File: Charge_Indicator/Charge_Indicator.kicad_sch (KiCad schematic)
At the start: 54 parts, among them J1 PZ254-2-02-S, J2 1711725, J3 1711725, SW1 SSSS811101, U1 TLV74033PDQNR

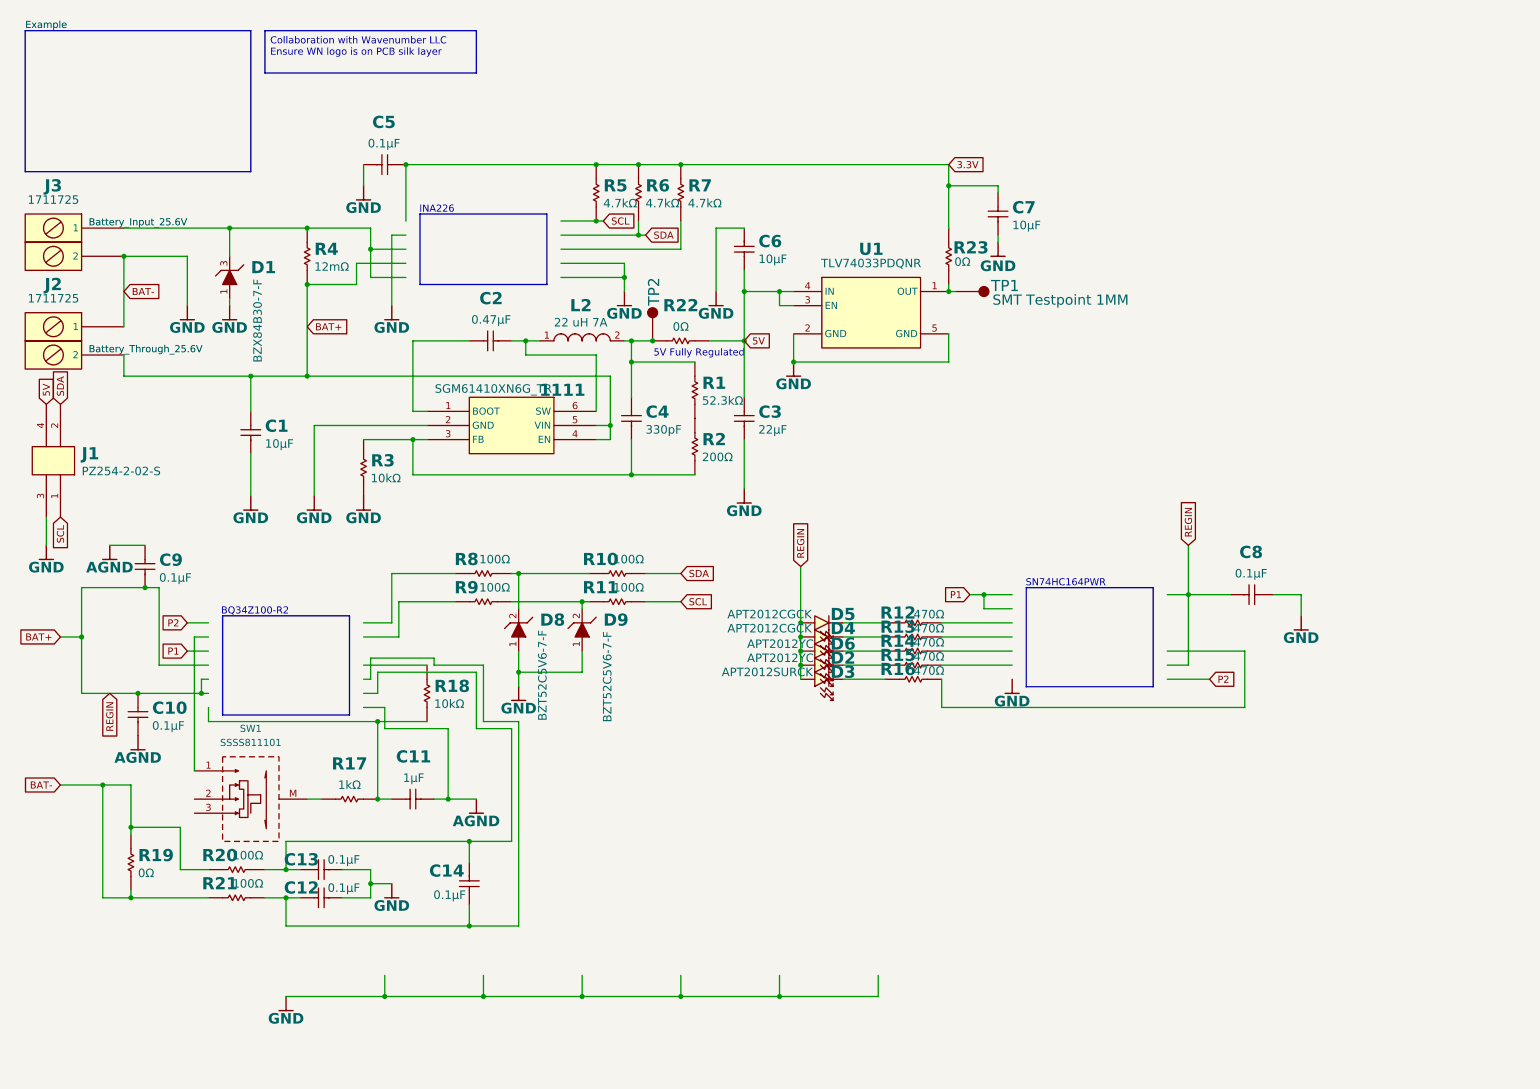
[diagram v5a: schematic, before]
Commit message: Many changes to the PCB schematic and PCB layout.
Summary of changes:
- Using new added chips to wn_pcb branch to connect up into KiCad automatically.
- Added another PZ254-2-02-S Dupont connection port for the 3v3 line, Alert pin, and HDQ highspeed data acquisition pin.
- Cleaned up the schematic a bit to make it less confusing.
- Added 0 Ohm resistors in front of both the buck and regulator so that 3v3 and 5v0 can be checked before real testing.
- EN pin of the SGM61410XN6G_TR is tied to VIN like stated in the datasheet.
- Test points added for the 3v3 and 5v0 outputs of both regulator and buck respectively.
- Fiducials and M3 mechanical holes added.
- Standardized the size of the PCB to 64mm x 64mm.
- Placed components in rough locations where they would be in the final revision.
- Spread out the components on the side (resistors, capacitors, zener diodes, etc.) such that they are easier to place into the PCB.
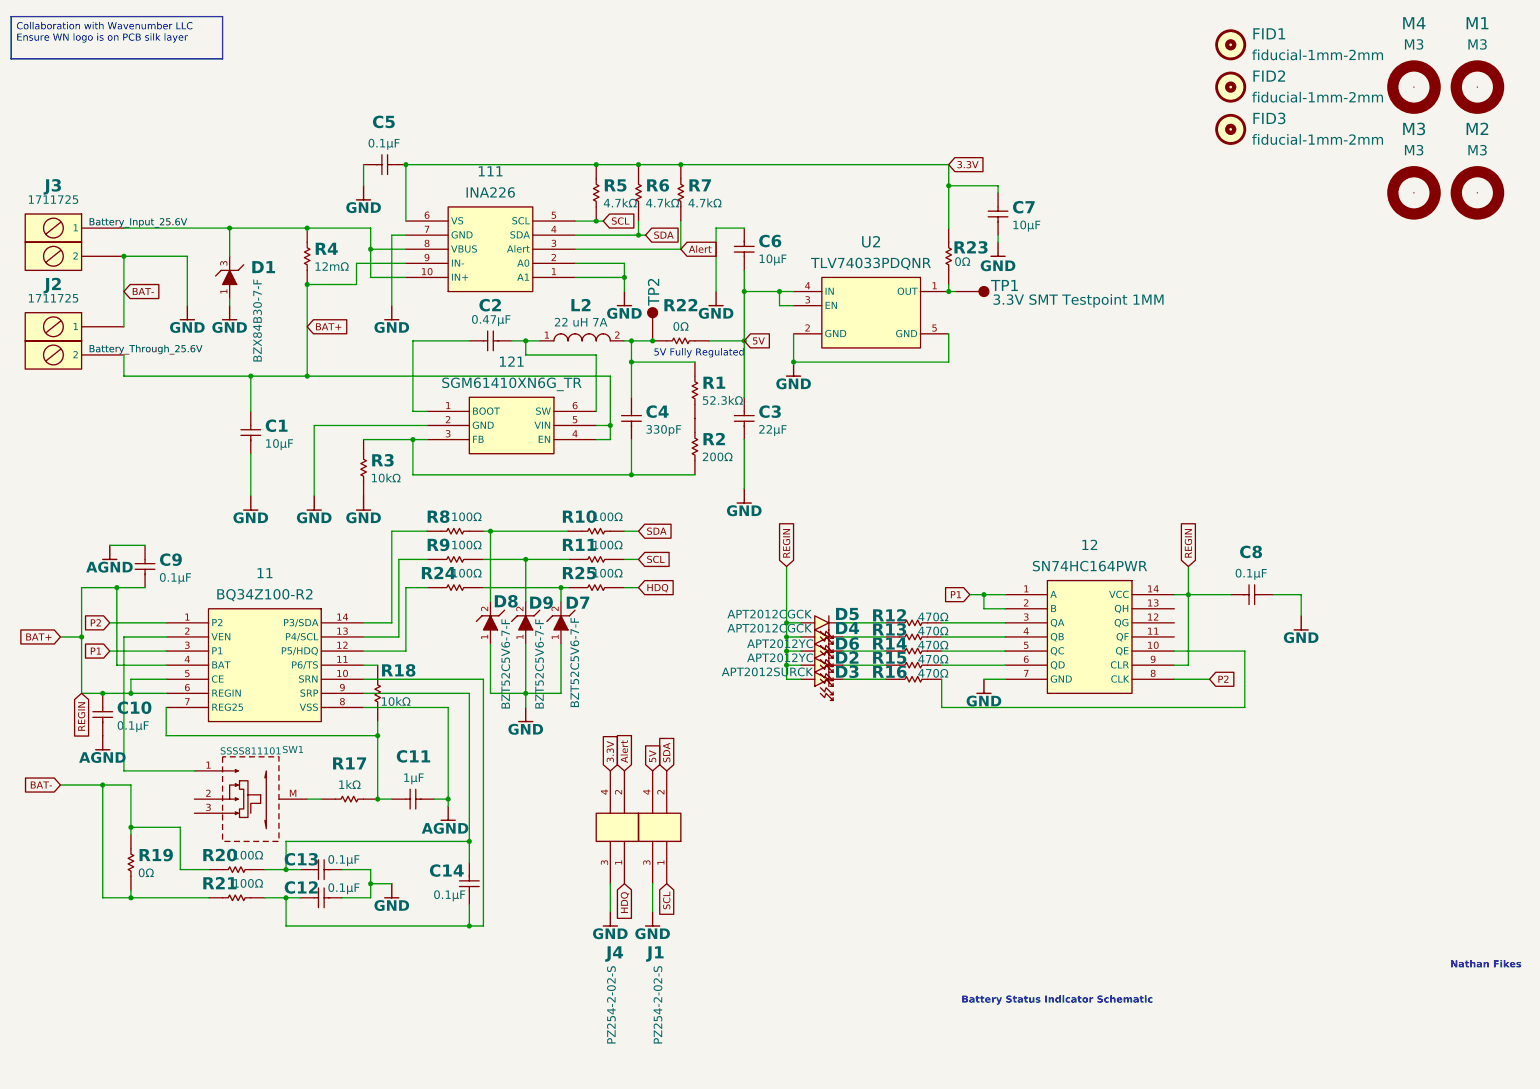
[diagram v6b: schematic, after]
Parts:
- removed 1111: SGM61410XN6G_TR, wavenumber:SGM61410XN6G_TR, symbol wn__wavenumber:SGM61410XN6G_TR
- removed U1: TLV74033PDQNR, symbol wavenumber:TLV74033PDQNR
- added 11: BQ34Z100-R2, wavenumber:BQ34Z100-R2, symbol wn__wavenumber:BQ34Z100-R2
- added 111: INA226, wavenumber:INA226, symbol wn__wavenumber:INA226
- added 12: SN74HC164PWR, wavenumber:SN74HC164PWR, symbol wn__wavenumber:SN74HC164PWR
- added 121: SGM61410XN6G_TR, wavenumber:SGM61410XN6G_TR, symbol wn__wavenumber:SGM61410XN6G_TR
- added D7: BZT52C5V6-7-F, wavenumber:D_SOD-123_P, symbol wn__wavenumber:DZ_1A_2C
- added FID1, FID2, FID3: fiducial-1mm-2mm, wavenumber:fiducial-1mm-2mm, symbol wn__wavenumber:fiducial
- added J4: PZ254-2-02-S, wavenumber:PZ254-2-02-S, symbol wn__wavenumber:CON-2-2
- added M1, M2, M3, M4: M3, wavenumber:M3, symbol wn__wavenumber:screw-hole
- added R24, R25: 100Ω, wavenumber:R0603_0.55MM_HD, symbol wn__wavenumber:R_2P
- added U2: TLV74033PDQNR, wavenumber:X2SON, symbol wn__wavenumber:TLV740XX
- TP1: value SMT Testpoint 1MM -> 3.3V SMT Testpoint 1MM
- TP2: value SMT Testpoint 1MM -> 5V SMT Testpoint 1MM
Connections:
- net 3.3V: now also 111.6 (VS), J4.4
- net 5V: now also U2.3 (EN), U2.4 (IN)
- net AGND: now also 11.8 (VSS)
- net BAT+: now also 11.4 (BAT), 11.5 (CE), 11.6 (REGIN), 111.9 (IN-), 12.14 (VCC), 12.9 (CLR), 121.4 (EN), 121.5 (VIN)
- net GND: now also 111.1 (A1), 111.2 (A0), 111.7 (GND), 12.7 (GND), 121.2 (GND), D7.1 (A), J4.3, U2.2 (GND), U2.5 (GND)
- net P1: now also 11.3 (P1), 12.1 (A), 12.2 (B)
- net P2: now also 11.1 (P2), 12.8 (CLK)
- net SCL: now also 111.5 (SCL)
- net SDA: now also 111.4 (SDA)
- net at C11.1, R17.2, R18.1: now also 11.7 (REG25)
- net at C12.1, C14.1, R21.2: now also 11.10 (SRN)
- net at C13.1, C14.2 (1), R20.2: now also 11.9 (SRP)
- net at R23.1, TP1.1: now also U2.1 (OUT)
- net at R15.2: now also 12.6 (QD)
- net at D1.3 (K), J3.1, R4.1: now also 111.10 (IN+), 111.8 (VBUS)
- net at R9.1: now also 11.13 (P4/SCL)
- net at C2.1: now also 121.1 (BOOT)
- net at C4.2 (1), R2.2, R3.1: now also 121.3 (FB)
- net at C2.2 (1), L2.1: now also 121.6 (SW)
- net at R13.2: now also 12.4 (QB)
- net at R8.1: now also 11.14 (P3/SDA)
- net at R18.2: now also 11.11 (P6/TS)
- net at R16.2: now also 12.10 (QE)
- net at R14.2: now also 12.5 (QC)
- net at R12.2: now also 12.3 (QA)
- net at SW1.1: now also 11.2 (VEN)
- net Alert: now reaches R7.2
- net Alert: now also 111.3 (Alert), J4.2
- new net: D7.2 (K), R24.2, R25.1
- new net: 11.12 (P5/HDQ), R24.1
- new net HDQ: J4.1, R25.2
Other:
- note added: "Battery Status Indicator Schematic"
- note added: "Nathan Fikes"
- note removed: "BQ34Z100-R2"
- note removed: "INA226"
- note removed: "SN74HC164PWR"
- moved on the sheet: C10, D8, D9, J1, R10, R11, R18, R8, R9

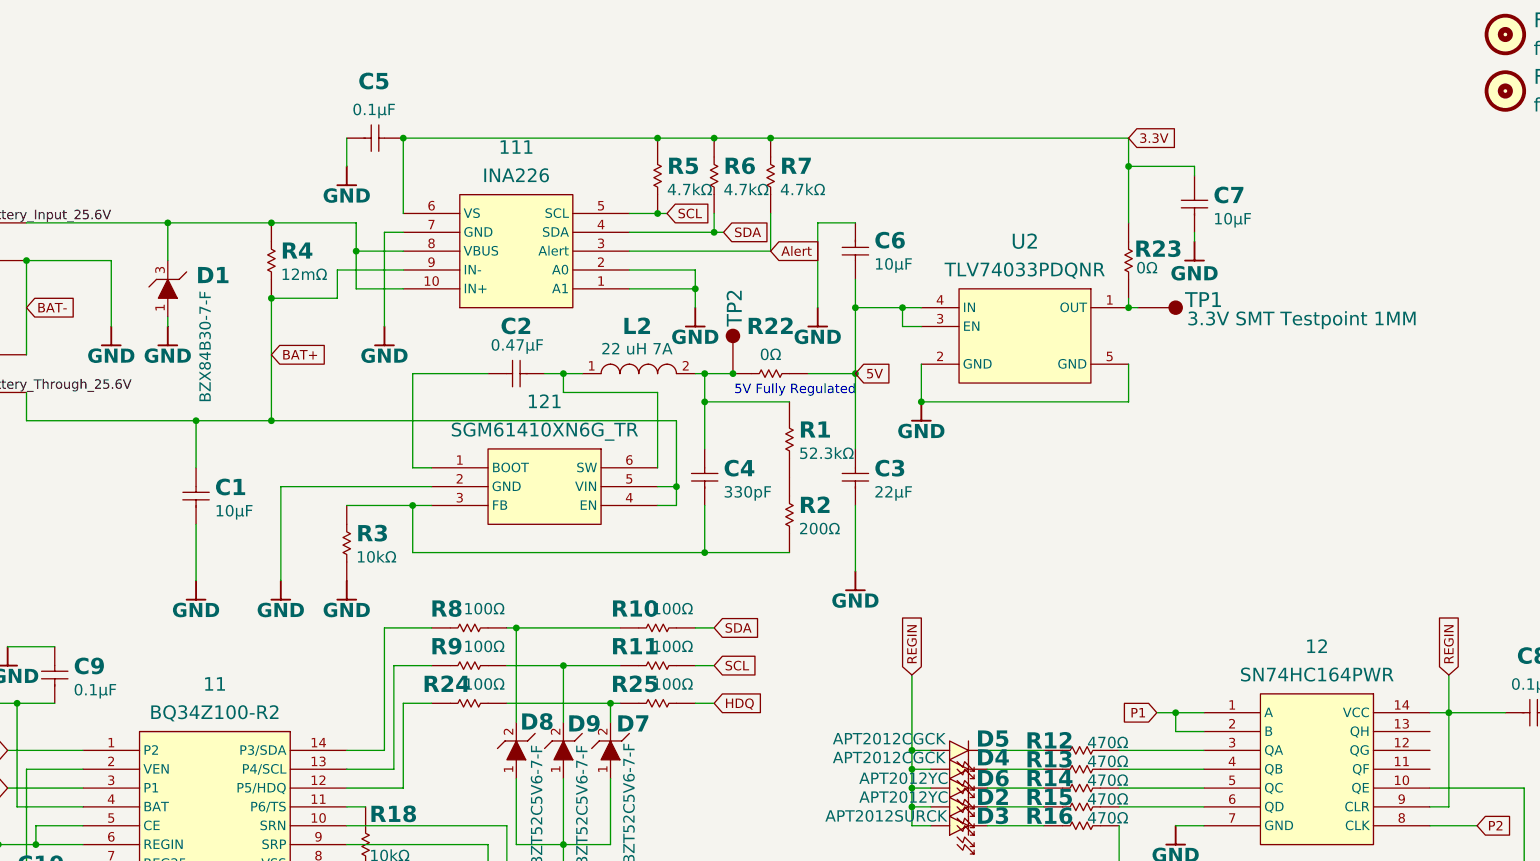
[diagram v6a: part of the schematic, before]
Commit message: Linking up local libraries
Linking up the symbols and footprints using local libraries for this project.
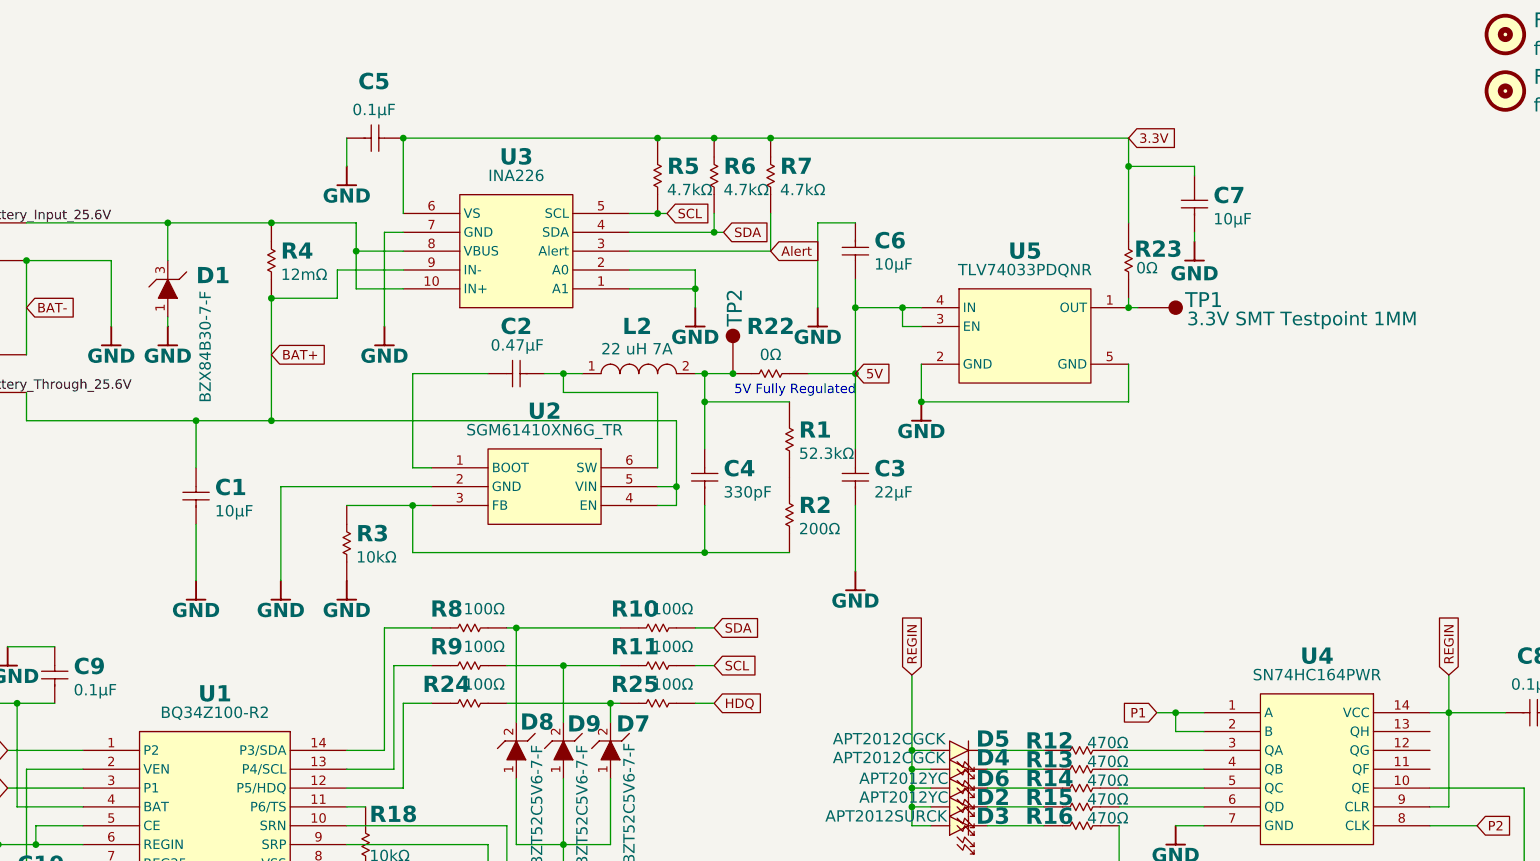
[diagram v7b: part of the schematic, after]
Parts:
- removed 11: BQ34Z100-R2, wavenumber:BQ34Z100-R2, symbol wn__wavenumber:BQ34Z100-R2
- removed 111: INA226, wavenumber:INA226, symbol wn__wavenumber:INA226
- removed 12: SN74HC164PWR, wavenumber:SN74HC164PWR, symbol wn__wavenumber:SN74HC164PWR
- removed 121: SGM61410XN6G_TR, wavenumber:SGM61410XN6G_TR, symbol wn__wavenumber:SGM61410XN6G_TR
- removed U2: TLV74033PDQNR, wavenumber:X2SON, symbol wn__wavenumber:TLV740XX
- added U1: BQ34Z100-R2, autonav_fp:BQ34Z100-R2, symbol BQ34Z100-R2:BQ34Z100-R2
- added U2: SGM61410XN6G_TR, autonav_fp:SGM61410XN6G_TR, symbol SGM61410XN6G_TR:SGM61410XN6G_TR
- added U3: INA226, autonav_fp:INA226, symbol INA226:INA226
- added U4: SN74HC164PWR, autonav_fp:SN74HC164PWR, symbol SN74HC164PWR:SN74HC164PWR
- added U5: TLV74033PDQNR, symbol TLV74033PDQNR:TLV74033PDQNR
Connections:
- net 3.3V: now also U3.6 (VS)
- net 5V: now also U5.3 (EN), U5.4 (IN)
- net AGND: now also U1.8 (VSS)
- net Alert: now also U3.3 (Alert)
- net BAT+: now also U1.4 (BAT), U1.5 (CE), U1.6 (REGIN), U2.4 (EN), U2.5 (VIN), U3.9 (IN-), U4.14 (VCC), U4.9 (CLR)
- net GND: now also U2.2 (GND), U3.1 (A1), U3.2 (A0), U3.7 (GND), U4.7 (GND), U5.2 (GND), U5.5 (GND)
- net P1: now also U1.3 (P1), U4.1 (A), U4.2 (B)
- net P2: now also U1.1 (P2), U4.8 (CLK)
- net SCL: now also U3.5 (SCL)
- net SDA: now also U3.4 (SDA)
- net at C11.1, R17.2, R18.1: now also U1.7 (REG25)
- net at C12.1, C14.1, R21.2: now also U1.10 (SRN)
- net at C13.1, C14.2 (1), R20.2: now also U1.9 (SRP)
- net at R23.1, TP1.1: now also U5.1 (OUT)
- net at R15.2: now also U4.6 (QD)
- net at D1.3 (K), J3.1, R4.1: now also U3.10 (IN+), U3.8 (VBUS)
- net at R16.2: now also U4.10 (QE)
- net at R12.2: now also U4.3 (QA)
- net at R13.2: now also U4.4 (QB)
- net at R14.2: now also U4.5 (QC)
- net at R9.1: now also U1.13 (P4/SCL)
- net at C2.1: now also U2.1 (BOOT)
- net at C2.2 (1), L2.1: now also U2.6 (SW)
- net at R8.1: now also U1.14 (P3/SDA)
- net at C4.2 (1), R2.2, R3.1: now also U2.3 (FB)
- net at R18.2: now also U1.11 (P6/TS)
- net at R24.1: now also U1.12 (P5/HDQ)
- net at SW1.1: now also U1.2 (VEN)

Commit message: WIP routing
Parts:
- U5: footprint (none) -> autonav_fp:TLV74033PDQNR
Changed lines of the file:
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@@
 			)
 		)
-		(property "Footprint" ""
+		(property "Footprint" "autonav_fp:TLV74033PDQNR"
 			(at 153.67 62.23 0)
 			(effects
